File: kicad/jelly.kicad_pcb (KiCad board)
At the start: 2 copper layers, 59.9 x 32.9 mm, 30 parts, among them M1 PAGER_MOTOR, M2 PAGER_MOTOR, P1 CONN_01X01, P10 CONN_01X01, P11 CONN_01X01, P12 CONN_01X01, P13 CONN_01X01, P14 CONN_01X01, P15 CONN_01X01, P2 CONN_01X01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

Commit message: Switch to low side switch and layout about
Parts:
- removed D3: D_Small, KiCad/Diodes_ThroughHole.pretty:Diode_DO-41_SOD81_Horizontal_RM10
- added PHOTO1: Photores, custom:ldr, F.Cu at (163.1, 69.8)
- added PHOTO2: Photores, custom:ldr, F.Cu at (137.1, 69.8)
- added Q3: Q_NMOS_SGD, KiCad/TO_SOT_Packages_THT.pretty:TO-92_Rugged, F.Cu at (139.3, 78.4)
- added RV1: POT, KiCad/Potentiometers.pretty:Potentiometer_Triwood_RM-065, F.Cu at (136.5, 74.5)
- added RV2: POT, KiCad/Potentiometers.pretty:Potentiometer_Triwood_RM-065, F.Cu at (166.7, 75.3)
- added SW1: SPST, KiCad/Pin_Headers.pretty:Pin_Header_Straight_1x02, B.Cu at (149.2, 79.3)
- DNP2, DNP3: moved to B.Cu
- Q1, Q2: value 2N7000 -> Q_NMOS_SGD
- R1: value Photores -> 1k; footprint custom:ldr -> KiCad/Discret.pretty:R3-5
- R2: value 220 -> 120
- R3: value Photores -> 100k; footprint custom:ldr -> KiCad/Discret.pretty:R3-5
- R4: value R -> 120
- moved R2 19.5 mm to (140.5, 84.7)
- moved R4 16.2 mm to (152.2, 84.8), turned to 180 degrees
- moved Q1 9.39 mm to (146.7, 76.0), turned to 0 degrees
- moved DNP3 5.06 mm to (163.1, 72.2)
- moved Q2 4.35 mm to (153.7, 78.8)
- moved BT1 3.97 mm to (149.5, 66.8), turned to 180 degrees
- moved R1 3.95 mm to (142.8, 71.8), turned to 0 degrees
- moved R3 2.97 mm to (155.6, 71.8), turned to 180 degrees
- moved DNP2 2.26 mm to (137.0, 72.2)
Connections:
- BT1 pad 1: Net-(BT1-Pad1) -> VCC
- BT1 pad 2: GND -> Net-(BT1-Pad2)
- M1 pad 2: Vout1 -> Vout2
- M2 pad 2: Vout2 -> Vout1
- Q1 pad 3: Vout1 -> Net-(BT1-Pad2)
- Q2 pad 2: Net-(Q2-Pad2) -> Net-(PHOTO2-Pad1)
- R1 pad 1: Net-(Q1-Pad2) -> Net-(R1-Pad1)
- R1 pad 2: VCC -> Net-(Q1-Pad2)
- R3 pad 1: Net-(Q2-Pad2) -> Net-(Q1-Pad2)
- R3 pad 2: VCC -> GND
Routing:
- net VCC: track 23.5 -> 0.48 mm
- net Vout2: track 1.90 -> 0.00 mm

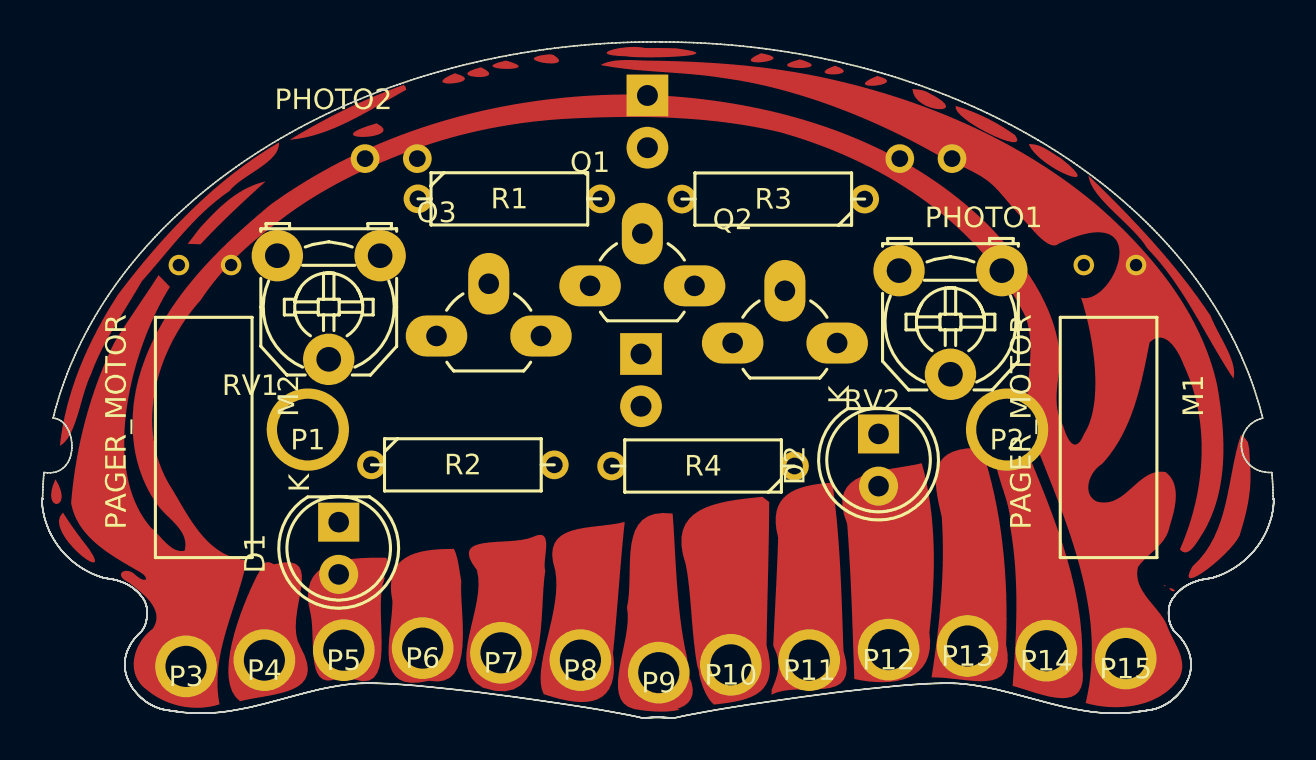
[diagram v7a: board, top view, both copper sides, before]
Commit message: Make jelly get out of the way
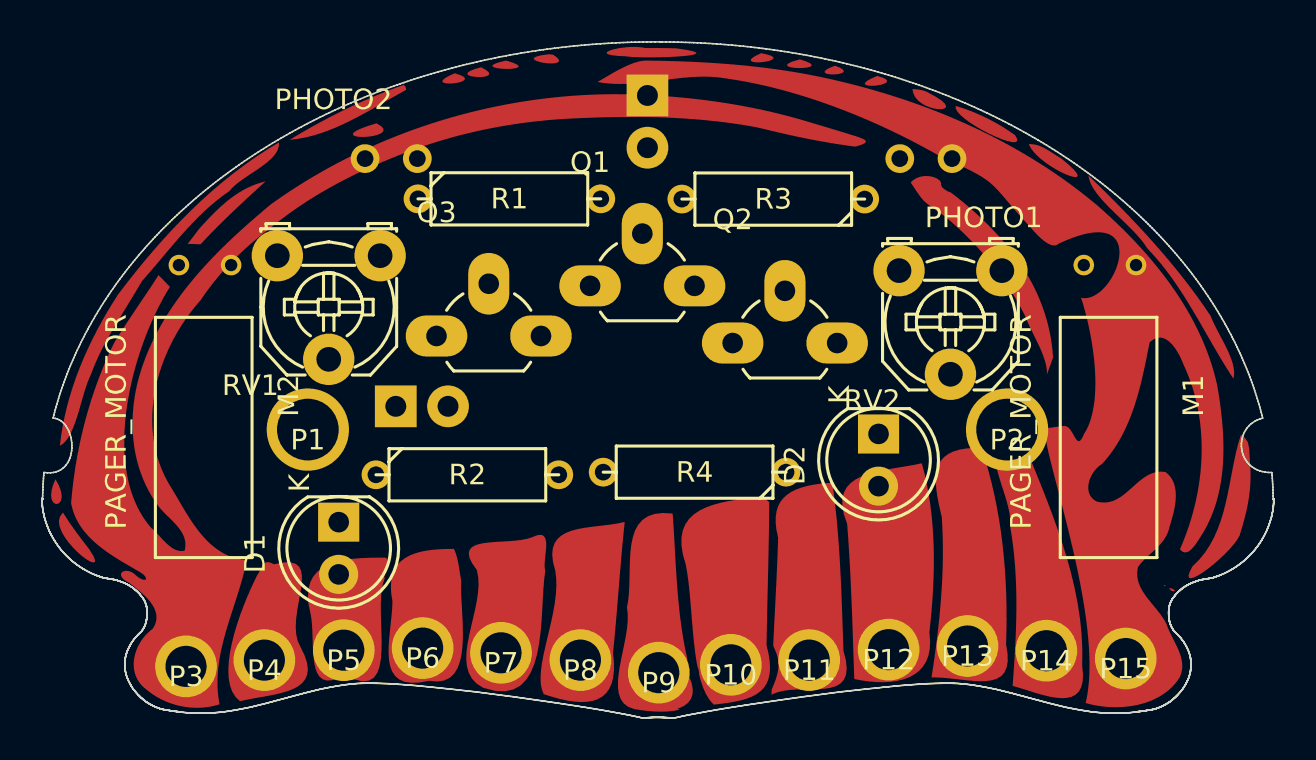
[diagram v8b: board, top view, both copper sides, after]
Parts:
- moved SW1 12.2 mm to (137.3, 81.9), turned to 270 degrees
- moved R2 0.53 mm to (140.8, 85.2)
- moved R4 0.51 mm to (151.8, 85.1)
